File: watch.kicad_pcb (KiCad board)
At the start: 2 copper layers, 35 x 34 mm, 70 parts, among them CON1 USB-MICRO-B, P1 CONN_6, SW1 SW_PUSH, SW2 SW_PUSH, SW3 SW_PUSH, SW4 SW_PUSH, U1 nrf51822, U2 ER-OLED015-1, U3 S25FL1-K, U4 74AHC1G14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

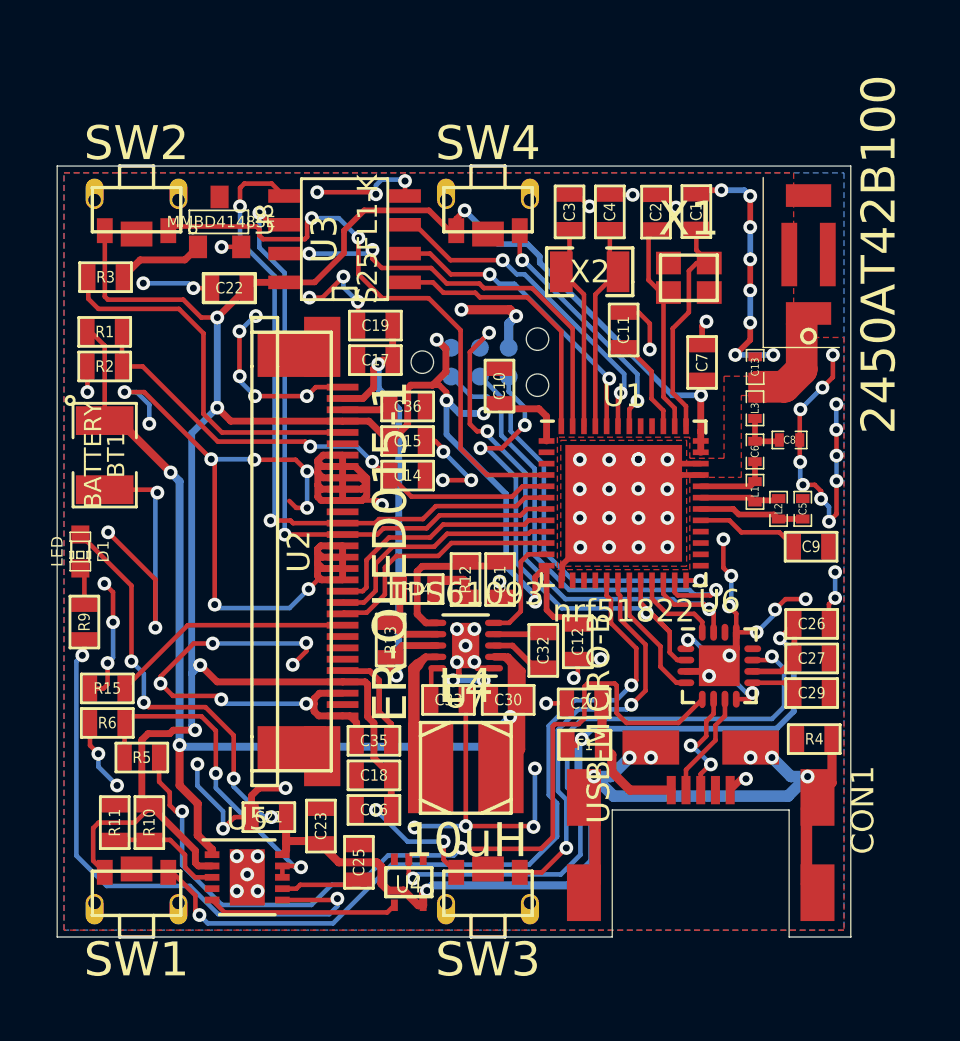
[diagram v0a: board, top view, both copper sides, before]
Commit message: Added testpoints, adjusted silkscreen texts
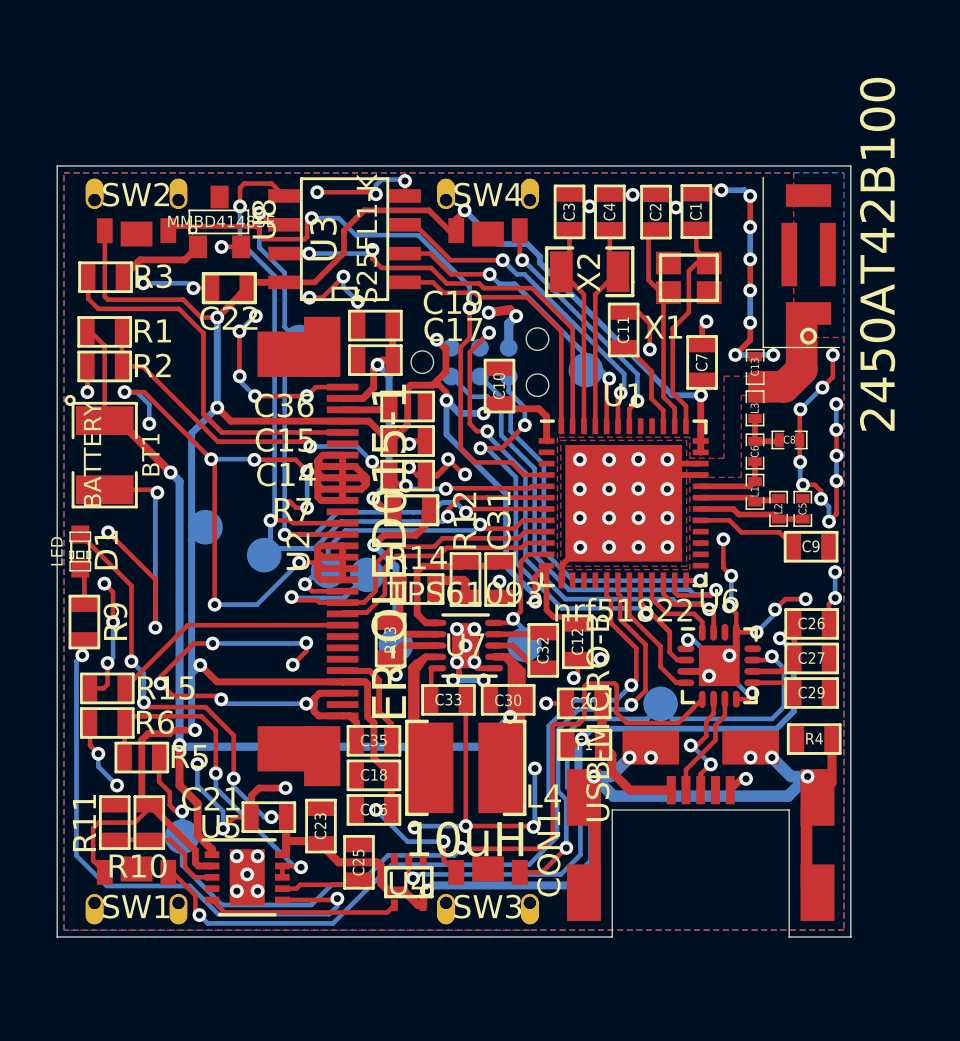
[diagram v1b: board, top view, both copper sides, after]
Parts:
- added R7: 0, SMD_Packages:SMD-0603, F.Cu at (75.6, 75.2)
- added TP10: TST, Measurement_Points:Measurement_Point_Round-SMD-Pad_Small, B.Cu at (86.6, 83.7)
- added TP11: TST, Measurement_Points:Measurement_Point_Round-SMD-Pad_Small, B.Cu at (74.9, 81.1)
- added TP2: TST, Measurement_Points:Measurement_Point_Round-SMD-Pad_Small, B.Cu at (69.1, 77.2)
- added TP3: TST, Measurement_Points:Measurement_Point_Round-SMD-Pad_Small, B.Cu at (70.7, 67.8)
- added TP4: TST, Measurement_Points:Measurement_Point_Round-SMD-Pad_Small, B.Cu at (83.3, 69.0)
- added TP5: TST, Measurement_Points:Measurement_Point_Round-SMD-Pad_Small, B.Cu at (72.0, 77.9)
- added TP6: TST, Measurement_Points:Measurement_Point_Round-SMD-Pad_Small, B.Cu at (73.7, 78.0)
- added TP7: TST, Measurement_Points:Measurement_Point_Round-SMD-Pad_Small, B.Cu at (80.6, 81.1)
- added TP8: TST, Measurement_Points:Measurement_Point_Round-SMD-Pad_Small, B.Cu at (66.5, 75.9)
- added TP9: TST, Measurement_Points:Measurement_Point_Round-SMD-Pad_Small, B.Cu at (65.5, 89.6)
- U2: footprint Omat:ER-OLED-CON30-BOTTOM-CONTACT -> ER-OLED-CON30-BOTTOM-CONTACT
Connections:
- R13 pad 2: 12.5V -> Net-(R13-Pad2)
- U7 pad 8: 12.5V -> Net-(R13-Pad2)
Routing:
- net Net-(R13-Pad2): track 0.00 -> 13.8 mm, vias 0 -> 2
- net MOSI: track 30.3 -> 40.5 mm, vias 2 -> 3
- net 12.5V: track 22.6 -> 13.2 mm
- net DC_DISP: track 11.1 -> 18.6 mm, vias 0 -> 1
- net /MISO: track 13.4 -> 19.7 mm
- net GND: track 241.7 -> 236.3 mm
- net RST_DISP: track 11.1 -> 15.2 mm, vias 0 -> 2
- net SCK: track 28.6 -> 32.7 mm, vias 2 -> 3
- net +3.3V: track 133.4 -> 135.4 mm
- net DISP_EN: track 4.85 -> 6.44 mm, vias 0 -> 1
- net Net-(C35-Pad1): track 4.68 -> 5.86 mm
- net Net-(R3-Pad1): track 16.7 -> 17.8 mm
- net /watch_usb_power/~PWREN: track 38.9 -> 40.0 mm
- net CS_DISP: track 11.0 -> 12.0 mm
- net /SW2: track 26.6 -> 27.3 mm
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
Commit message: Minor modifications
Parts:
- ANT1: footprint Omat:ANTENNA_2.4GHz_SMD_2450AT42B100 -> ANTENNA_2.4GHz_SMD_2450AT42B100
- moved BT1 0.13 mm to (62.2, 72.8)
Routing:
- net GND: track 236.3 -> 239.5 mm
- net +3.3V: track 135.4 -> 134.1 mm
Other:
- rule pad_to_mask_clearance: 0 -> 0.1
- board text added: "BLE HRM WATCH V1.0"
